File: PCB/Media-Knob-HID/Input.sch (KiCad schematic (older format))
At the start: 35 parts, among them SW1 PCB_Switch_Winkel_THT, SW2 PCB_Switch_Winkel_THT, SW3 PCB_Switch_Winkel_THT, SW4 PCB_Switch_Winkel_THT, SW5 PCB_Switch_Winkel_THT, SW6 Rotary_stehend_THT

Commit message: Umbau auf mehrere Platinen
Umbau auf 2 Paltinen
- HID Paltine
- USB Platine
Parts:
- renumbered C31 to C33, C32 to C34, C33 to C35, C34 to C36, C35 to C37, C36 to C38, C37 to C39, C38 to C40, R8 to R10, R9 to R11, R10 to R12, R11 to R13, R12 to R14, R13 to R15, R14 to R16, R15 to R17, R16 to R18, R17 to R19, R5 to R7, R6 to R8, R7 to R9
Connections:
- net labels added: +3.3V
- net labels removed: VCC

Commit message: Interface und Powersupply
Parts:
- renumbered C33 to C301, C34 to C302, C35 to C303, C36 to C304, C37 to C305, C38 to C306, C39 to C307, C40 to C308, R7 to R301, R8 to R302, R9 to R303, R10 to R304, R11 to R305, R12 to R306, R13 to R307, R14 to R308, R15 to R309, R16 to R310, R17 to R311, R18 to R312, R19 to R313, SW1 to SW301, SW2 to SW302, SW3 to SW303, SW4 to SW304, SW5 to SW305, SW6 to SW306, TP28 to TP301, TP29 to TP302, TP30 to TP303, TP31 to TP304, TP32 to TP305, TP33 to TP306, TP34 to TP307, TP35 to TP308
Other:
- moved on the sheet: C301, C302, C303, C304, C305, C306, C307, C308, R301, R302, R303, R304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

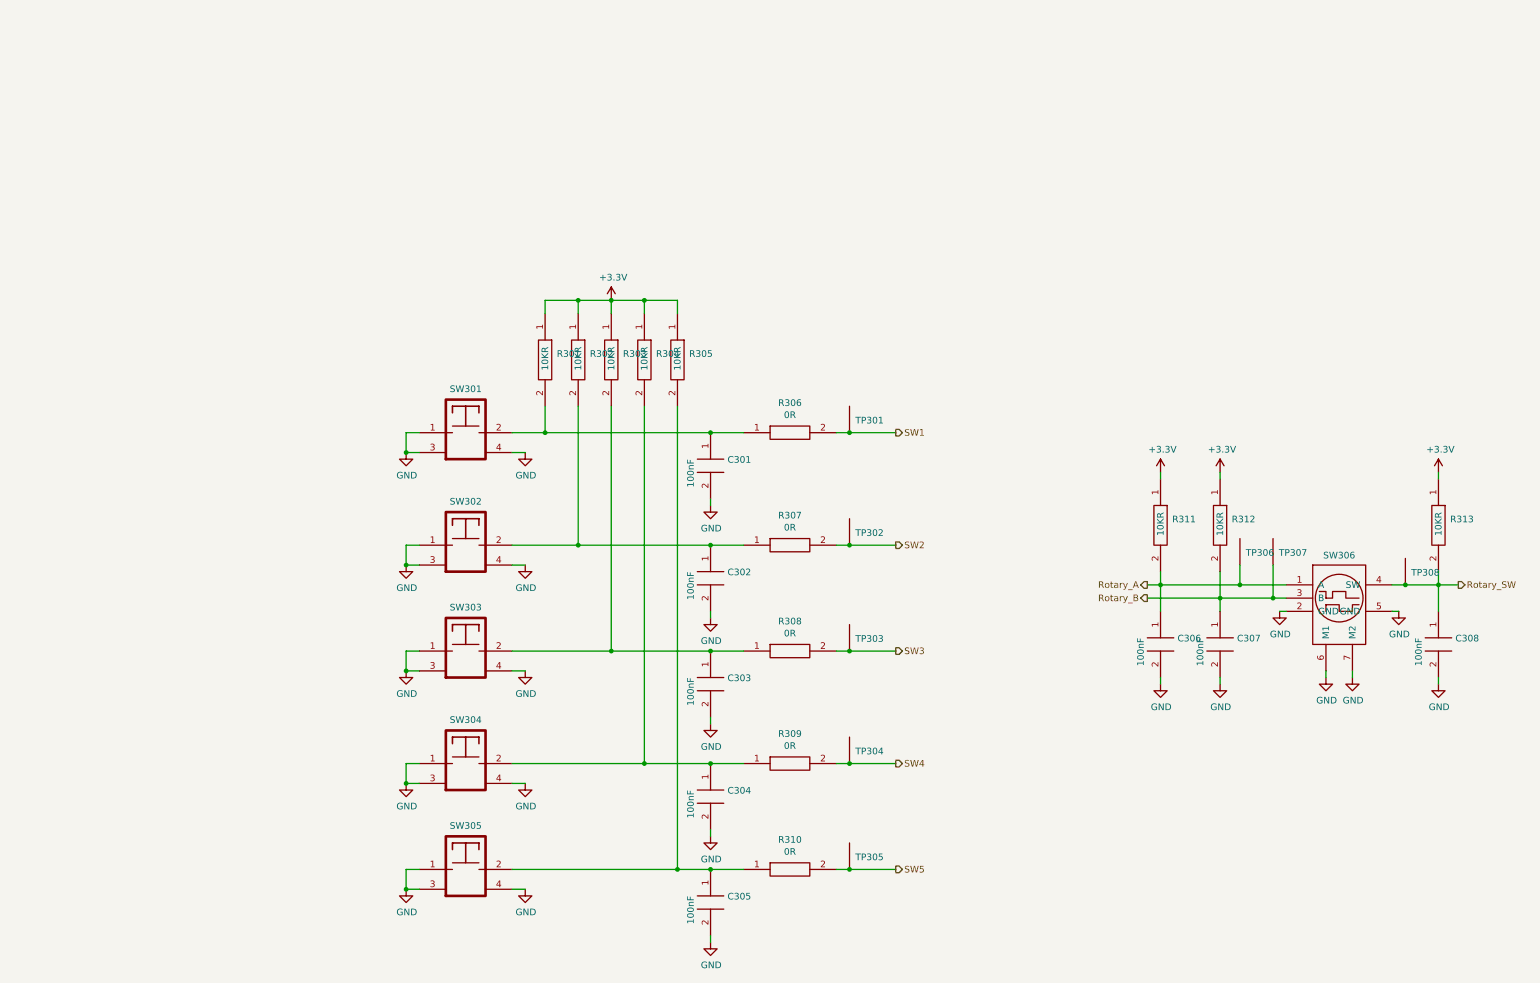
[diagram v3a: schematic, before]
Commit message: Media_knob an neues Konzept angepasst
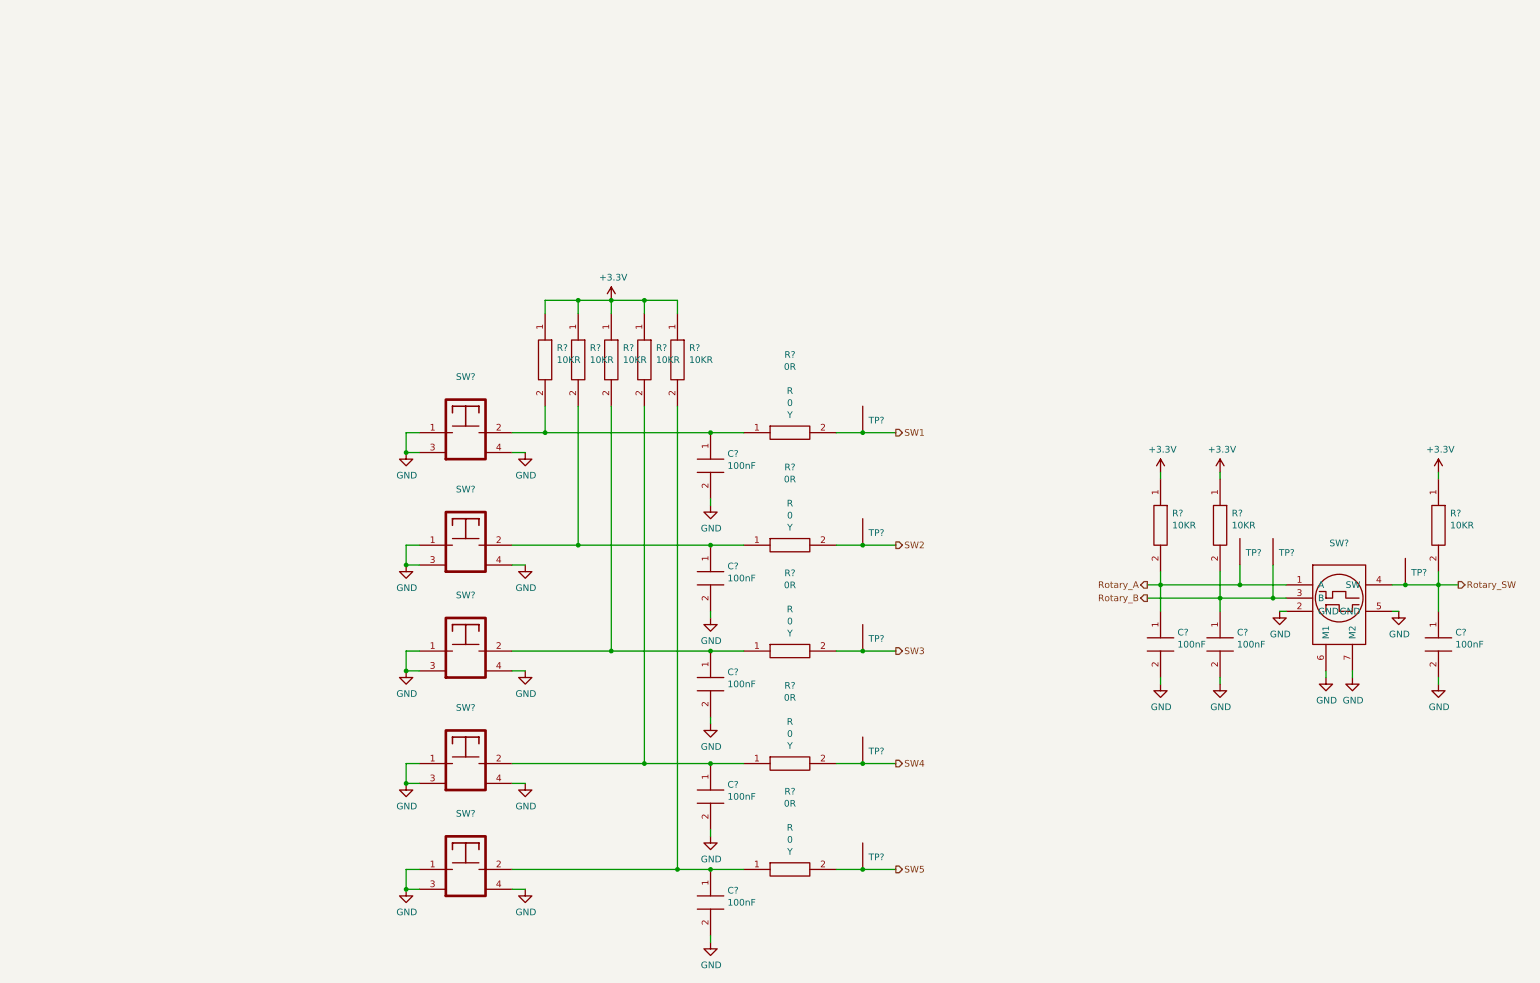
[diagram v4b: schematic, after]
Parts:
- removed C301, C302, C303, C304, C305, C306, C307, C308: 100n_0603, Kondensator:CAPC1608, symbol Kondensator:100n_0603
- removed R301, R302, R303, R304, R305, R311, R312, R313: 10K_0603, Widerstand:RESC1608, symbol Widerstand:10K_0603
- removed R306, R307, R308, R309, R310: 0R_0603, Widerstand:RESC1608, symbol Widerstand:0R_0603
- removed SW301, SW302, SW303, SW304, SW305: PCB_Switch_Winkel_THT, Artikel:PCB_Switch_Winkel_THT, symbol Artikel:PCB_Switch_Winkel_THT
- removed SW306: Rotary_stehend_THT, Artikel:Rotary_stehend_THT, symbol Artikel:Rotary_stehend_THT
- removed TP301, TP302, TP303, TP304, TP305, TP306, TP307, TP308: TP_100, Technik:TP100, symbol Technik:TP_100
- added C? (x8): 100n_0603, Kondensator:CAPC1608, symbol _Kondensator:100n_0603
- added R? (x5): 0R_0603, Widerstand:RESC1608, symbol _Widerstand:0R_0603
- added R? (x8): 10K_0603, Widerstand:RESC1608, symbol _Widerstand:10K_0603
- added SW?: Rotary_stehend_THT, Artikel:Rotary_stehend_THT, symbol _Artikel:Rotary_stehend_THT
- added SW? (x5): PCB_Switch_Winkel_THT, Artikel:PCB_Switch_Winkel_THT, symbol _Artikel:PCB_Switch_Winkel_THT
- added TP? (x8): TP_100, Technik:TP100;, symbol _Technik:TP_100
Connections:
- net +3V3: now also R?.1, R?.1, R?.1, R?.1, R?.1, R?.1, R?.1, R?.1
- net GND: now also C?.2, C?.2, C?.2, C?.2, C?.2, C?.2, C?.2, C?.2, SW?.1, SW?.1, SW?.1, SW?.1, SW?.1, SW?.2 (GND), SW?.3, SW?.3, SW?.3, SW?.3, SW?.3, SW?.4, SW?.4, SW?.4, SW?.4, SW?.4, SW?.5 (GND), SW?.6 (M1), SW?.7 (M2)
- net Rotary_A: now also C?.1, R?.2, SW?.1 (A), TP?.1
- net Rotary_B: now also C?.1, R?.2, SW?.3 (B), TP?.1
- net Rotary_SW: now also C?.1, R?.2, SW?.4 (SW), TP?.1
- net SW1: now also R?.2, TP?.1
- net SW2: now also R?.2, TP?.1
- net SW3: now also R?.2, TP?.1
- net SW4: now also R?.2, TP?.1
- net SW5: now also R?.2, TP?.1
- new net: C?.1, R?.1, R?.2, SW?.2 (x5)
